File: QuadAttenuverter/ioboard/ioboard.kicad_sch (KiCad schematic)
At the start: 38 parts, among them J1 Conn_01x09, J2 Conn_02x10_Counter_Clockwise

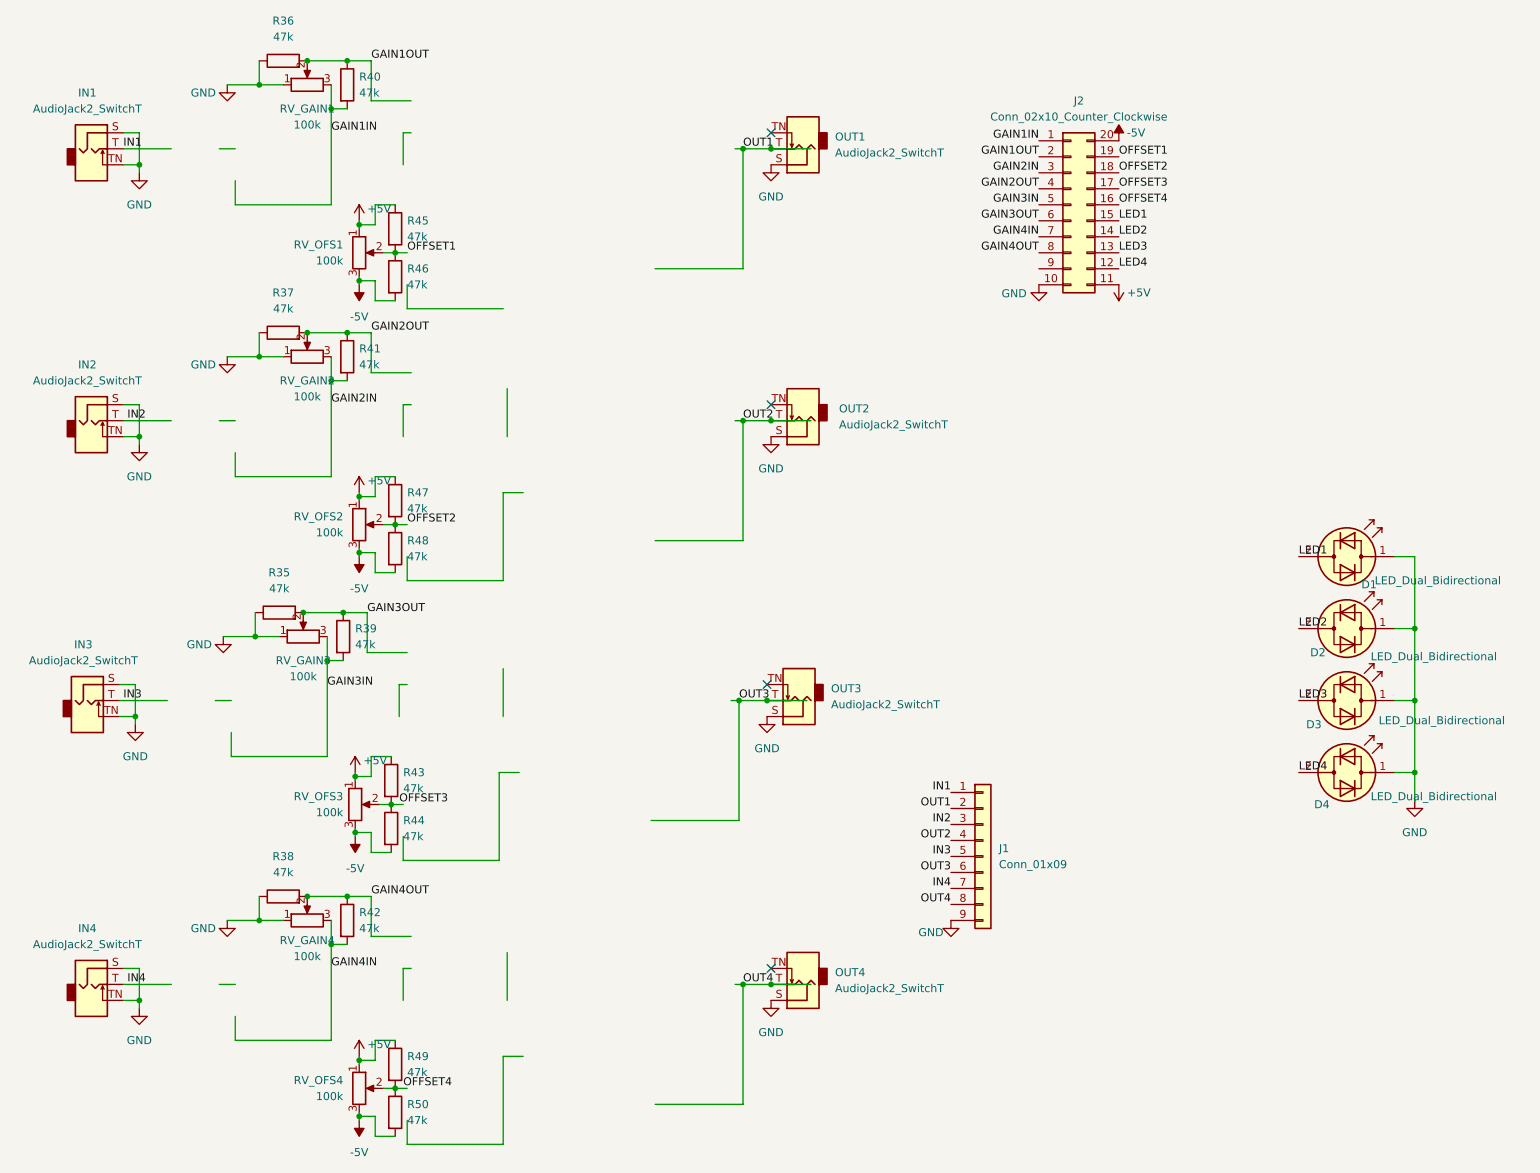
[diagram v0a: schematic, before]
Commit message: Initial kibot export integration
And small fixes in the ioboard to remove the warnings.
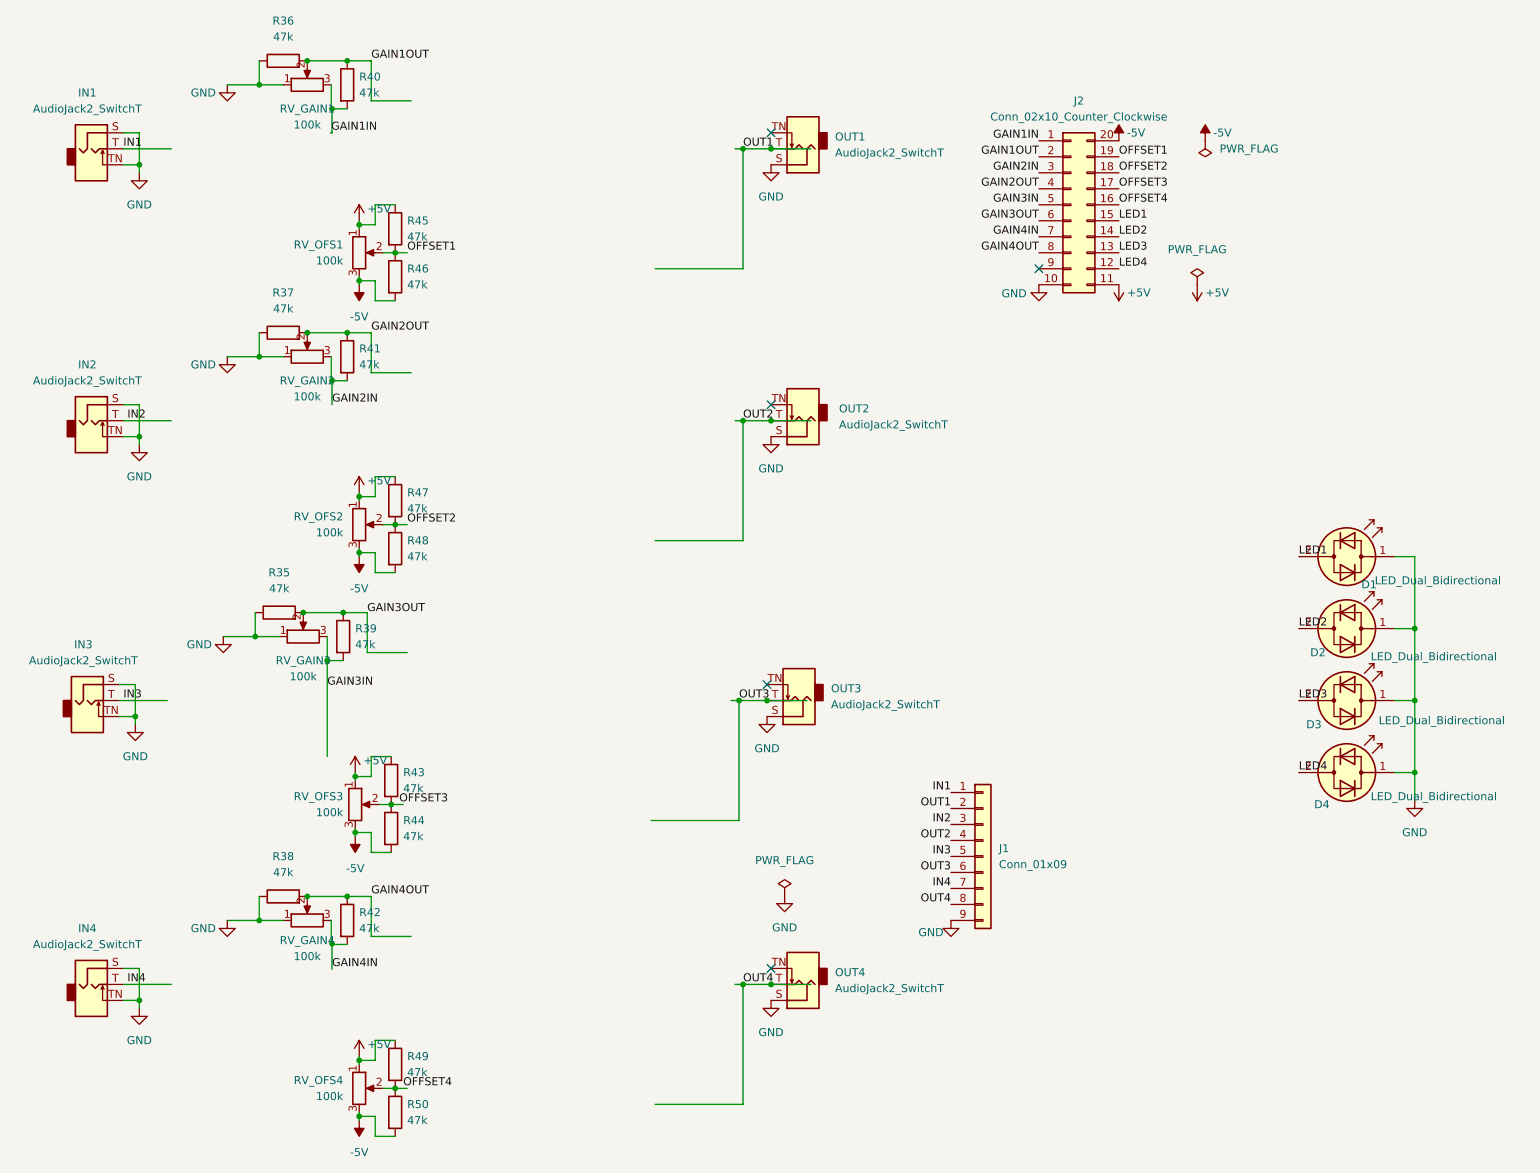
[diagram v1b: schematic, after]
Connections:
- net GAIN4IN: no longer R42.2, RV_GAIN4.3
- new net: R42.2, RV_GAIN4.3
- no-connect marks 4 -> 5

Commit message: Fix the pinout of the offset POTs so right is plus
These were reversed (it's an inverting amplifier) in the original
design. Also added a marking to the board.
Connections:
- net GAIN1IN: now also RV_GAIN1.1; no longer RV_GAIN1.3
- net GAIN2IN: now also RV_GAIN2.1; no longer RV_GAIN2.3
- net GAIN3IN: now also RV_GAIN3.1; no longer RV_GAIN3.3
- net GAIN4IN: now also R42.2, RV_GAIN4.1
- net GND: now also RV_GAIN1.3, RV_GAIN2.3, RV_GAIN3.3, RV_GAIN4.3; no longer RV_GAIN1.1, RV_GAIN2.1, RV_GAIN3.1, RV_GAIN4.1
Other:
- moved on the sheet: RV_GAIN1, RV_GAIN2, RV_GAIN3, RV_GAIN4
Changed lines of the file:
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@@
   (junction (at 45.085 74.93) (diameter 0) (color 0 0 0 0)
   )
+  (junction (at 75.565 155.575) (diameter 0) (color 0 0 0 0)
+  )
   (junction (at 44.45 119.38) (diameter 0) (color 0 0 0 0)
   )
@@
   )
   (junction (at 85.725 178.435) (diameter 0) (color 0 0 0 0)
-  )
-  (junction (at 75.692 155.448) (diameter 0) (color 0 0 0 0)
   )
   (no_connect (at 145.415 26.67))
@@
     (stroke (width 0) (type default) (color 0 0 0 0))
   )
+  (wire (pts (xy 75.565 155.575) (xy 75.565 159.385))
+    (stroke (width 0) (type default) (color 0 0 0 0))
+  )
   (wire (pts (xy 83.82 178.435) (xy 85.725 178.435))
     (stroke (width 0) (type default) (color 0 0 0 0))
@@
     (stroke (width 0) (type default) (color 0 0 0 0))
   )
-  (wire (pts (xy 75.692 155.448) (xy 75.692 159.512))
-    (stroke (width 0) (type default) (color 0 0 0 0))
-  )
   (wire (pts (xy 64.135 19.05) (xy 67.945 19.05))
     (stroke (width 0) (type default) (color 0 0 0 0))
@@
     (effects (font (size 1.27 1.27)) (justify right bottom))
   )
-  (label "GAIN4IN" (at 75.692 159.512 0)
+  (label "GAIN4IN" (at 75.565 159.385 0)
     (effects (font (size 1.27 1.27)) (justify left bottom))
   )
@@
     (pin "2")
   )
-  (symbol (lib_id "Device:R_Potentiometer") (at 71.755 62.23 90) (unit 1)
+  (symbol (lib_id "Device:R_Potentiometer") (at 71.755 62.23 270) (mirror x) (unit 1)
     (in_bom yes) (on_board yes) (fields_autoplaced)
     (property "Reference" "RV_GAIN2" (id 0) (at 71.755 66.04 90))
@@
     (pin "2")
   )
-  (symbol (lib_id "Device:R_Potentiometer") (at 71.755 19.05 90) (unit 1)
+  (symbol (lib_id "Device:R_Potentiometer") (at 71.755 19.05 270) (mirror x) (unit 1)
     (in_bom yes) (on_board yes) (fields_autoplaced)
     (property "Reference" "RV_GAIN1" (id 0) (at 71.755 22.86 90))
@@
     (pin "3")
   )
-  (symbol (lib_id "Device:R_Potentiometer") (at 71.755 151.765 90) (unit 1)
+  (symbol (lib_id "Device:R_Potentiometer") (at 71.755 151.765 270) (mirror x) (unit 1)
     (in_bom yes) (on_board yes) (fields_autoplaced)
     (property "Reference" "RV_GAIN4" (id 0) (at 71.755 154.94 90))
@@
     (pin "1")
   )
-  (symbol (lib_id "Device:R_Potentiometer") (at 71.12 106.68 90) (unit 1)
+  (symbol (lib_id "Device:R_Potentiometer") (at 71.12 106.68 270) (mirror x) (unit 1)
     (in_bom yes) (on_board yes) (fields_autoplaced)
     (property "Reference" "RV_GAIN3" (id 0) (at 71.12 110.49 90))
